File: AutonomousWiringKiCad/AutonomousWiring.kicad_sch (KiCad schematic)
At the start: 14 parts

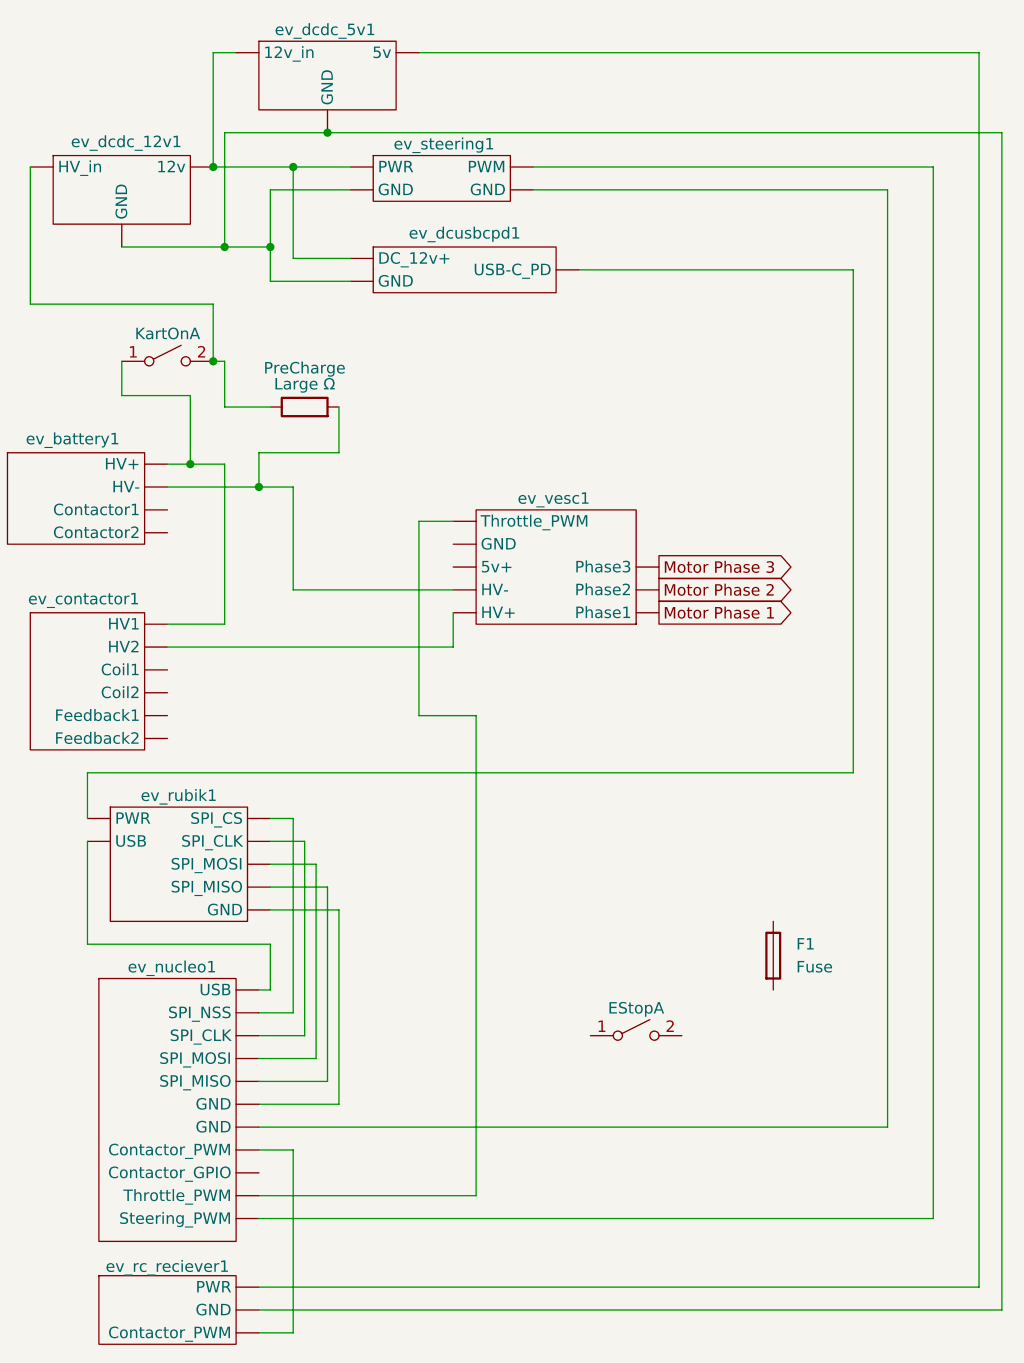
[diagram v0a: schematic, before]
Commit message: Trying to place fuse and contactor loop
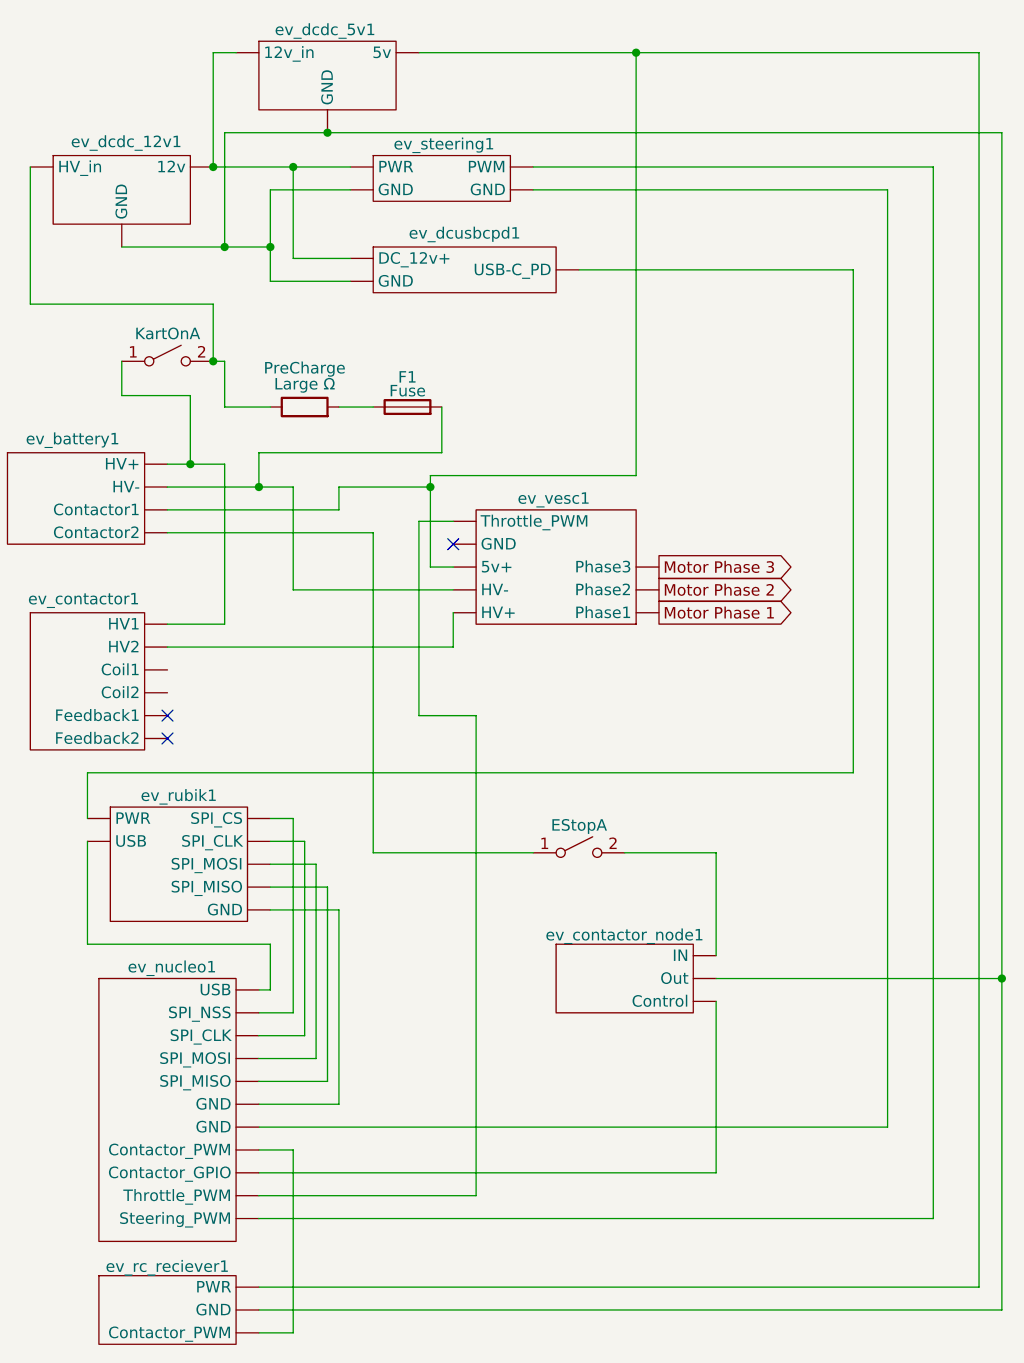
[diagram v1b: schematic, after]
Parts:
- added ev_contactor_node1: ~, symbol ev_kart:ev_contactor_node
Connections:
- net at ev_battery1. (Contactor2): now also EStop.1 (A)
- net at ev_dcdc_5v1. (5v), ev_rc_reciever1. (Contactor_PWM): now also ev_battery1. (Contactor2), ev_vesc1. (Throttle_PWM)
- net at ev_contactor1. (Feedback2): no longer ev_vesc1. (Throttle_PWM)
- net at ev_nucleo1. (Steering_PWM): now also ev_rubik1. (GND); no longer ev_vesc1. (Throttle_PWM)
- net at F1.1: now also PreCharge.2
- net at F1.2: now also ev_battery1. (Contactor2), ev_vesc1. (Throttle_PWM)
- net at ev_rubik1. (GND): now also ev_dcusbcpd1. (USB-C_PD); no longer ev_nucleo1. (Steering_PWM)
- net at EStop.2 (B): now also ev_contactor_node1. (Control)
- new net: ev_contactor_node1. (Control), ev_dcdc_12v1. (12v), ev_dcdc_5v1. (5v), ev_dcusbcpd1. (USB-C_PD), ev_rc_reciever1. (Contactor_PWM), ev_steering1. (GND)
- new net: ev_dcdc_12v1. (12v), ev_dcdc_5v1. (5v), ev_dcusbcpd1. (USB-C_PD), ev_steering1. (GND)
- new net: KartOn.1 (A), ev_battery1. (Contactor2), ev_contactor1. (Feedback2)
- new net: ev_contactor1. (Feedback2), ev_vesc1. (Throttle_PWM)
- new net: ev_nucleo1. (Steering_PWM), ev_vesc1. (Throttle_PWM)
- new net: ev_nucleo1. (Steering_PWM), ev_steering1. (GND)
- new net: ev_contactor_node1. (Control), ev_nucleo1. (Steering_PWM)
- new net: ev_nucleo1. (Steering_PWM), ev_rubik1. (GND) (x5)
- now unconnected: ev_contactor1. (Feedback2)
- no-connect marks 0 -> 3
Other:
- moved on the sheet: EStopA, F1

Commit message: Actually connect the coil in the contactor....
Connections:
- net at ev_contactor1. (Feedback2): now also ev_contactor_node1. (Control); no longer ev_vesc1. (Throttle_PWM)
- net at ev_nucleo1. (Steering_PWM): now also ev_rubik1. (GND); no longer ev_vesc1. (Throttle_PWM)
- net at ev_contactor_node1. (Control): now also EStop.2 (B); no longer ev_nucleo1. (Steering_PWM)
- net at ev_rubik1. (GND): now also ev_dcusbcpd1. (USB-C_PD); no longer ev_nucleo1. (Steering_PWM)
- new net: ev_contactor1. (Feedback2), ev_dcdc_12v1. (12v), ev_dcdc_5v1. (5v), ev_dcusbcpd1. (USB-C_PD), ev_rc_reciever1. (Contactor_PWM), ev_steering1. (GND)
- new net: ev_dcdc_12v1. (12v), ev_dcdc_5v1. (5v), ev_dcusbcpd1. (USB-C_PD), ev_steering1. (GND)
- new net: ev_battery1. (Contactor2), ev_dcdc_5v1. (5v), ev_rc_reciever1. (Contactor_PWM), ev_vesc1. (Throttle_PWM)
- new net: F1.2, ev_battery1. (Contactor2), ev_vesc1. (Throttle_PWM)
- new net: KartOn.1 (A), ev_battery1. (Contactor2), ev_contactor1. (Feedback2)
- new net: ev_contactor1. (Feedback2), ev_vesc1. (Throttle_PWM)
- new net: ev_nucleo1. (Steering_PWM), ev_vesc1. (Throttle_PWM)
- new net: ev_nucleo1. (Steering_PWM), ev_steering1. (GND)
- new net: ev_contactor_node1. (Control), ev_nucleo1. (Steering_PWM)
- new net: ev_nucleo1. (Steering_PWM), ev_rubik1. (GND) (x5)
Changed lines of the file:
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@@
 	)
 	(junction
-		(at 129.54 124.46)
+		(at 129.54 92.71)
 		(diameter 0)
 		(color 0 0 0 0)
@@
 	(wire
 		(pts
-			(xy 129.54 30.48) (xy 129.54 124.46)
+			(xy 129.54 30.48) (xy 129.54 92.71)
 		)
 		(stroke
@@
 	(wire
 		(pts
-			(xy 129.54 124.46) (xy 129.54 161.29)
-		)
-		(stroke
-			(width 0)
-			(type default)
-		)
-	)
-	(wire
-		(pts
 			(xy 71.12 95.25) (xy 71.12 148.59)
 		)
@@
 	(wire
 		(pts
-			(xy 97.79 124.46) (xy 129.54 124.46)
-		)
-		(stroke
-			(width 0)
-			(type default)
-		)
-	)
-	(wire
-		(pts
 			(xy 59.69 110.49) (xy 77.47 110.49)
 		)
@@
 	(wire
 		(pts
+			(xy 106.68 124.46) (xy 97.79 124.46)
+		)
+		(stroke
+			(width 0)
+			(type default)
+		)
+	)
+	(wire
+		(pts
 			(xy 46.99 148.59) (xy 71.12 148.59)
 		)
@@
 	(wire
 		(pts
+			(xy 36.83 90.17) (xy 106.68 90.17)
+		)
+		(stroke
+			(width 0)
+			(type default)
+		)
+	)
+	(wire
+		(pts
 			(xy 97.79 110.49) (xy 97.79 121.92)
 		)
@@
 	(wire
 		(pts
+			(xy 129.54 92.71) (xy 129.54 161.29)
+		)
+		(stroke
+			(width 0)
+			(type default)
+		)
+	)
+	(wire
+		(pts
 			(xy 41.91 55.88) (xy 41.91 49.53)
 		)
@@
 	(wire
 		(pts
+			(xy 36.83 92.71) (xy 129.54 92.71)
+		)
+		(stroke
+			(width 0)
+			(type default)
+		)
+	)
+	(wire
+		(pts
 			(xy 64.77 73.66) (xy 68.58 73.66)
 		)
@@
 		)
 		(stroke
+			(width 0)
+			(type default)
+		)
+	)
+	(wire
+		(pts
+			(xy 106.68 90.17) (xy 106.68 124.46)
+		)
+		(stroke

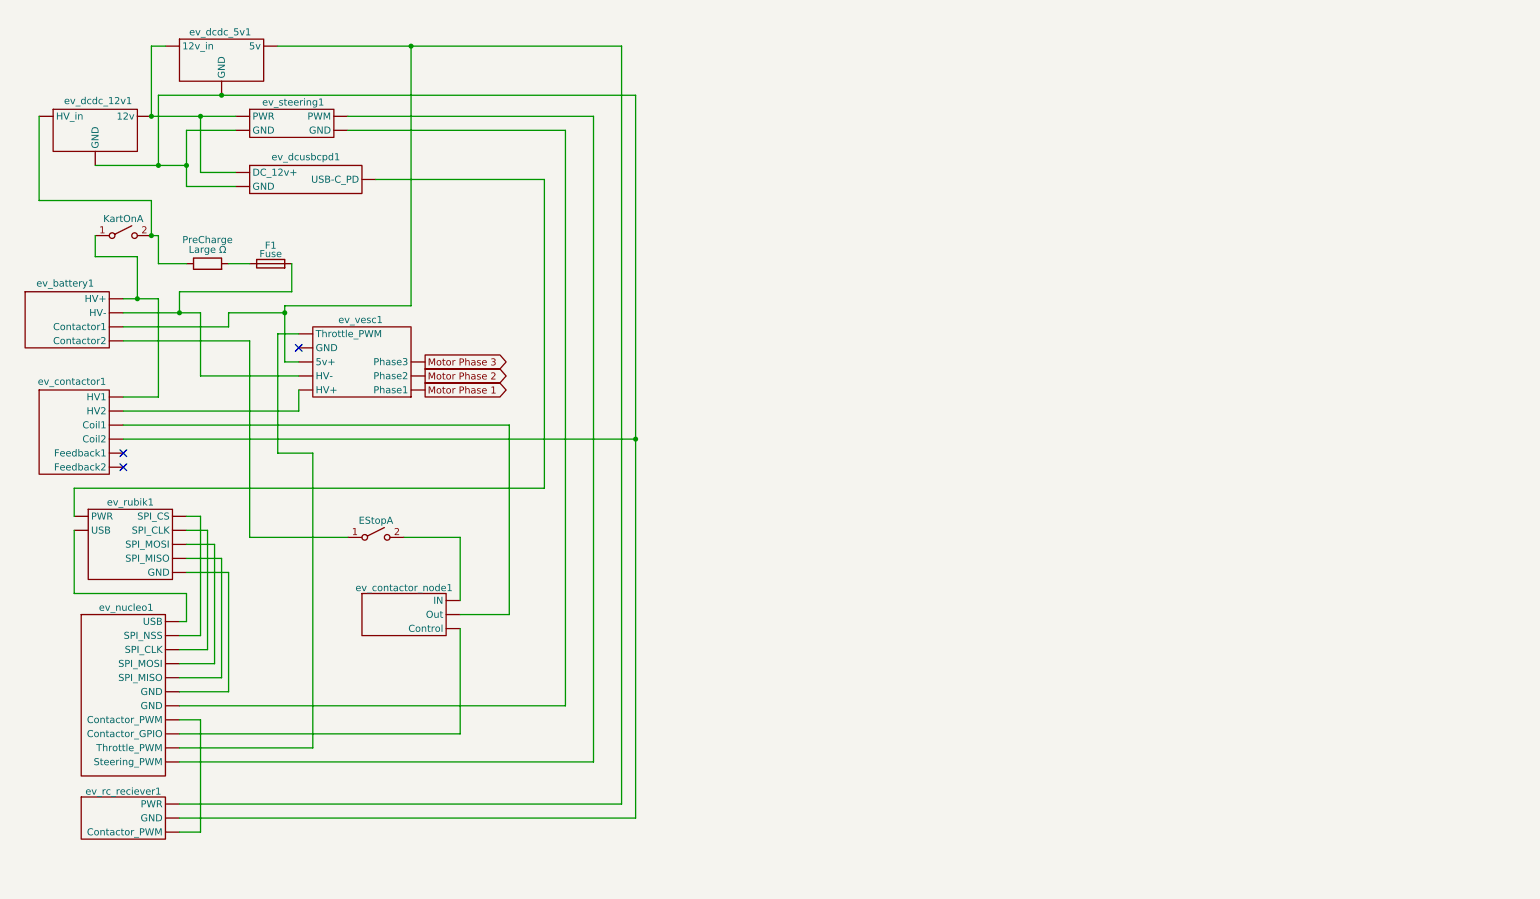
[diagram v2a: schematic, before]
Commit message: Starting a new draft. Contains positions, colors, guages, and hopefully 1 round of Jack feedback
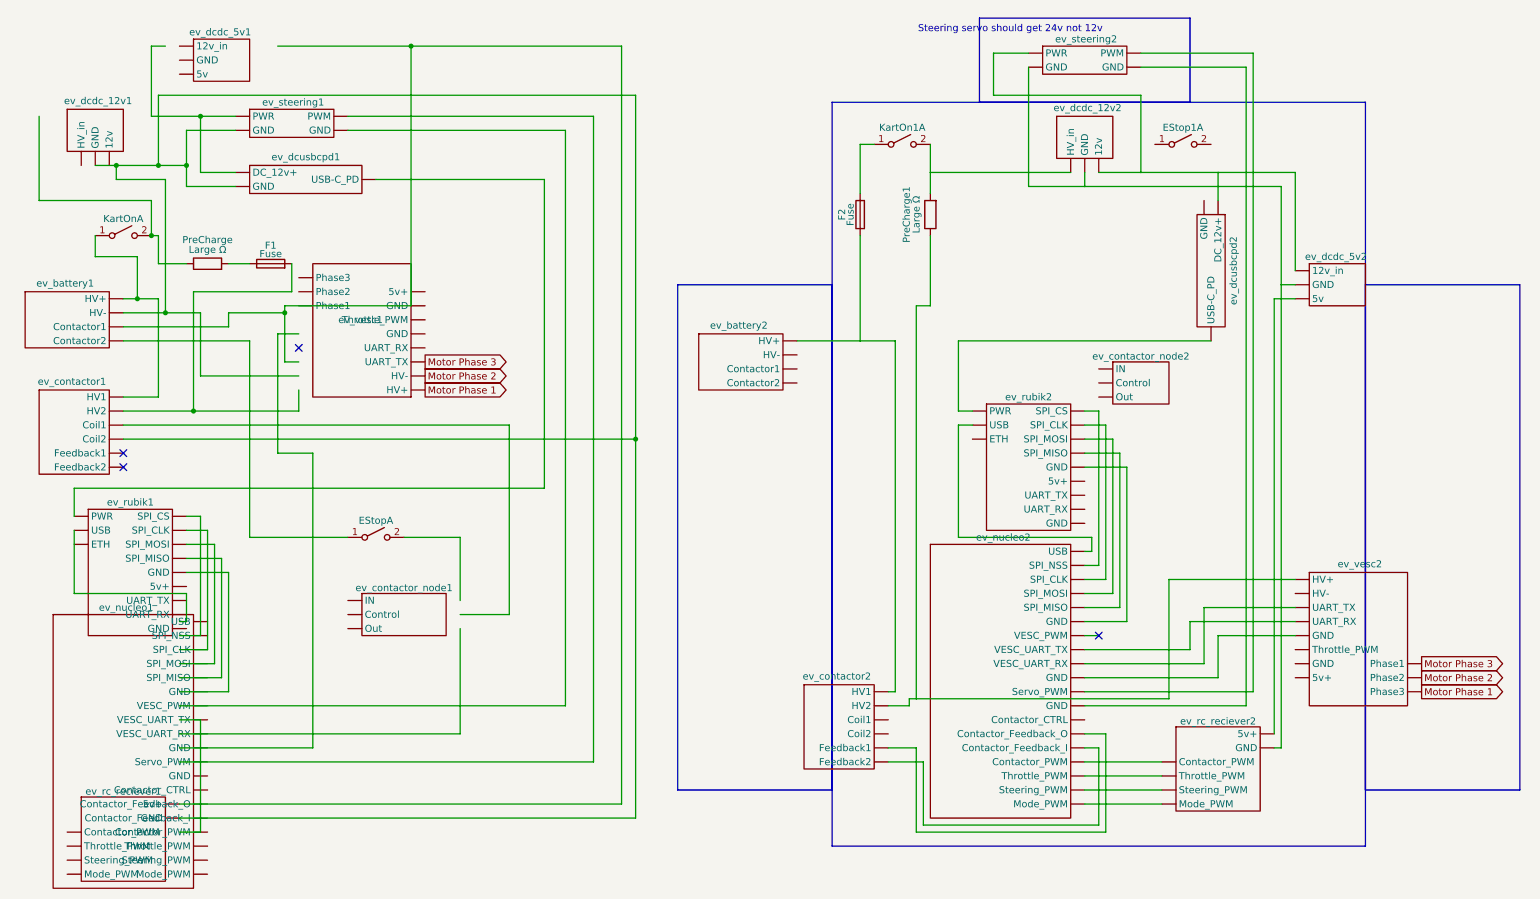
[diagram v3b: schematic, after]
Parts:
- added EStop1, KartOn1: SW_DPST_x2, symbol Switch:SW_DPST_x2
- added F2: Fuse, symbol Device:Fuse
- added PreCharge1: Large Ω, symbol Device:R
- added ev_battery2: ~, symbol ev_kart:ev_battery
- added ev_contactor2: ~, symbol ev_kart:ev_contactor
- added ev_contactor_node2: ~, symbol ev_kart:ev_contactor_node
- added ev_dcdc_12v2: ~, symbol ev_kart:ev_dcdc_12v
- added ev_dcdc_5v2: ~, symbol ev_kart:ev_dcdc_5v
- added ev_dcusbcpd2: ~, symbol ev_kart:ev_dcusbcpd
- added ev_nucleo2: ~, symbol ev_kart:ev_nucleo
- added ev_rc_reciever2: ~, symbol ev_kart:ev_rc_reciever
- added ev_rubik2: ~, symbol ev_kart:ev_rubik
- added ev_steering2: ~, symbol ev_kart:ev_steering
- added ev_vesc2: ~, symbol ev_kart:ev_vesc
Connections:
- net Motor Phase 1: now also ev_vesc2. (Phase3)
- net Motor Phase 2: now also ev_vesc2. (Phase3)
- net Motor Phase 3: now also ev_vesc2. (Phase3)
- net at KartOn.2 (B), PreCharge.1: no longer ev_dcdc_12v1. (12v)
- net at ev_contactor1. (Feedback2): no longer ev_vesc1. (Throttle_PWM)
- net at ev_nucleo1. (Mode_PWM): now also ev_rubik1. (GND); no longer ev_vesc1. (Throttle_PWM)
- net at ev_rc_reciever1. (GND): no longer ev_nucleo1. (Steering_PWM)
- net at ev_steering1. (GND): now also ev_dcusbcpd1. (USB-C_PD); no longer ev_nucleo1. (Steering_PWM)
- net at ev_contactor_node1. (Out): no longer ev_contactor1. (Feedback2)
- net at EStop.2 (B): no longer ev_contactor_node1. (Control)
- net at ev_rubik1. (GND): now also ev_dcusbcpd1. (USB-C_PD); no longer ev_nucleo1. (Steering_PWM)
- new net: ev_battery1. (Contactor2), ev_contactor1. (Feedback2), ev_dcdc_12v1. (12v), ev_dcusbcpd1. (USB-C_PD), ev_rc_reciever1. (GND), ev_steering1. (GND)
- new net: F2.2, KartOn1.1 (A)
- new net: KartOn1.2 (B), PreCharge1.2, ev_dcdc_12v2. (12v)
- new net: ev_battery1. (Contactor2), ev_rc_reciever1. (GND)
- new net: KartOn.1 (A), ev_battery1. (Contactor2), ev_contactor1. (Feedback2)
- new net: ev_nucleo2. (Mode_PWM), ev_steering2. (GND) (x2)
- new net: ev_contactor2. (Feedback2), ev_nucleo2. (Mode_PWM) (x2)
- new net: ev_nucleo2. (Mode_PWM), ev_rc_reciever2. (GND) (x4)
- new net: ev_nucleo2. (Mode_PWM), ev_rubik2. (GND) (x6)
- new net: ev_nucleo2. (Mode_PWM), ev_vesc2. (Phase3) (x3)
- new net: F2.1, ev_battery2. (Contactor2), ev_contactor2. (Feedback2)
- new net: ev_dcdc_12v2. (12v), ev_dcdc_5v2. (5v), ev_dcusbcpd2. (USB-C_PD), ev_steering2. (GND)
- new net: ev_dcdc_12v2. (12v), ev_dcdc_5v2. (5v), ev_rc_reciever2. (GND), ev_steering2. (GND)
- new net: ev_dcdc_5v2. (5v), ev_rc_reciever2. (GND)
- new net: F1.2, ev_contactor1. (Feedback2)
- new net: PreCharge1.1, ev_contactor2. (Feedback2), ev_vesc2. (Phase3)
- new net: ev_dcusbcpd2. (USB-C_PD), ev_rubik2. (GND)
- now unconnected: ev_contactor1. (Feedback2), ev_contactor1. (Feedback2), ev_contactor_node1. (Control), ev_dcdc_5v1. (5v), ev_dcdc_5v1. (5v), ev_dcdc_5v1. (5v), ev_rc_reciever1. (Contactor_PWM), ev_rc_reciever1. (Contactor_PWM)
- no-connect marks 3 -> 4
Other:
- note added: "Steering servo should get 24v not 12v"
- moved on the sheet: ev_contactor_node1, ev_dcdc_5v1
